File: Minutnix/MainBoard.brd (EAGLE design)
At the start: 108.8 x 69.7 mm, 32 parts, among them IC1 MEGA8-AI, Q1 32.768kHz

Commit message: Archivisation and actualisation
Archivisation of 1 version of boards
New version of boards
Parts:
- removed DRIVER1, DRIVER2: 74LS47N, 74xx-eu:DIL16
- added C5, C6, C7, C8: 0.1uF, rcl:140CLH-1010
- added IC2, IC3, IC4, IC5: TPIC6C596PW, tpic:SO16
- added LSDIGIT1, MSDIGIT1: LED-7-SEGM-56MM, BigLED7Segm:MYTHT
- added Q2: (no value), semicon-smd-ipc:SOT23
- added R16, R17, R18, R19, R20, R21, R22, R23, R24, R25, R26, R27, R28: 50, rcl:R01005
- added R29: 10k, rcl:R01005
- added R30: 4.7k, rcl:R01005
- added SG1: F/CM12P, buzzer:F/CM12P
- moved R15 121.8 mm to (100.0, -92.8), turned to 0 degrees
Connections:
- removed net N$33: IC1.9, R15.2
- removed net N$36: J_REG_9V_1.VOUT, LSDIGIT.COM1, LSDIGIT.COM8, MSDIGIT.COM1, MSDIGIT.COM8
- new net N$43: IC2.14, R8.2
- new net N$51: MSDIGIT1.A, R22.1
- new net N$52: MSDIGIT1.B, R23.1
- new net N$53: MSDIGIT1.C, R24.1
- new net N$54: MSDIGIT1.D, R25.1
- new net N$55: MSDIGIT1.E, R26.1
- new net N$56: MSDIGIT1.F, R27.1
- new net N$57: MSDIGIT1.G, R28.1
- new net N$58: IC3.3, R9.2
- new net N$59: IC3.4, R10.2
- new net N$60: IC3.5, R11.2
- new net N$61: IC3.6, R12.2
- new net N$62: IC3.11, R13.2
- new net N$63: IC3.12, R14.2
- new net N$64: IC3.13, R15.2
- new net N$65: IC3.14, R16.2
- new net N$66: IC4.3, R17.2
- new net N$67: IC4.4, R18.2
- new net N$68: IC4.5, R19.2
- new net N$69: IC4.6, R20.2
- new net N$70: IC4.11, R21.2
- new net N$71: IC4.12, R22.2
- new net N$72: IC4.13, R23.2
- new net N$73: IC4.14, R24.2
- new net N$74: IC5.3, R25.2
- new net N$75: IC5.4, R26.2
- new net N$76: IC5.5, R27.2
- new net N$77: IC5.6, R28.2
- new net N$78: IC3.9, IC4.2
- new net N$79: IC4.9, IC5.2
- new net N$80: IC2.9, IC3.2
- net GND: now also C5.-, C6.-, C7.-, C8.-, IC2.16, IC3.16, IC4.16, IC5.16, Q2.2; no longer DRIVER1.8, DRIVER2.8
- net N$10: now also IC2.12; no longer DRIVER1.15
- net N$11: now also IC2.13; no longer DRIVER1.14
- net N$21: now also Q2.1, R30.1; no longer DRIVER2.6, IC1.17, USBASP.3
- net N$23: now also IC2.2; no longer DRIVER2.1, USBASP.4
- net N$24: now also IC2.7, IC3.7, IC4.7, IC5.7, R29.1; no longer DRIVER2.2, IC1.16, USBASP.1
- net N$26: now also IC1.17, IC2.15, IC3.15, IC4.15, IC5.15, USBASP.3; no longer DRIVER1.7, IC1.23
- net N$27: now also IC1.16, IC2.10, IC3.10, IC4.10, IC5.10, USBASP.1; no longer DRIVER1.1, IC1.24
- net N$28: now also J_REG_9V_1.VOUT, LSDIGIT.COM1, LSDIGIT.COM8, LSDIGIT1.COM1, LSDIGIT1.COM8, MSDIGIT.COM1, MSDIGIT.COM8, MSDIGIT1.COM1, MSDIGIT1.COM8; no longer DRIVER1.2, IC1.25
- net N$29: now also Q2.3, SG1.-; no longer DRIVER1.6, IC1.26
- net N$3: now also IC1.13, R30.2; no longer DRIVER2.7, IC1.12
- net N$32: no longer R15.1
- net N$4: now also IC1.14, IC2.8, IC3.8, IC4.8, IC5.8; no longer DRIVER1.4, DRIVER2.4, IC1.13
- net N$44: now also LSDIGIT1.A, R15.1; no longer DRIVER2.14, R14.2
- net N$45: now also LSDIGIT1.B, R16.1; no longer DRIVER2.15, R13.2
- net N$46: now also LSDIGIT1.C, R17.1; no longer DRIVER2.9, R12.2
- net N$47: now also LSDIGIT1.D, R18.1; no longer DRIVER2.10, R11.2
- net N$48: now also LSDIGIT1.E, R19.1; no longer DRIVER2.11, R10.2
- net N$49: now also LSDIGIT1.F, R20.1; no longer DRIVER2.12, R9.2
- net N$5: now also IC2.3; no longer DRIVER1.13
- net N$50: now also LSDIGIT1.G, R21.1; no longer DRIVER2.13, R8.2
- net N$6: now also IC2.4; no longer DRIVER1.12
- net N$7: now also IC2.5; no longer DRIVER1.11
- net N$8: now also IC2.6; no longer DRIVER1.10
- net N$9: now also IC2.11; no longer DRIVER1.9
- net VCC: now also C5.+, C6.+, C7.+, C8.+, IC2.1, IC3.1, IC4.1, IC5.1, R29.2, SG1.+; no longer DRIVER1.16, DRIVER2.16
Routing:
- net N$36: track 205.8 -> 0.00 mm
- net N$28: track 0.00 -> 198.0 mm
- net N$45: track 49.2 -> 0.00 mm
- net N$44: track 43.9 -> 0.00 mm
- net N$50: track 43.6 -> 0.00 mm
- net N$46: track 41.9 -> 0.00 mm
- net N$49: track 41.8 -> 0.00 mm
- net N$3: track 37.9 -> 0.00 mm
- net N$47: track 27.8 -> 0.00 mm
- net N$4: track 26.8 -> 0.00 mm
- net N$48: track 23.4 -> 0.00 mm
- net VCC: track 151.9 -> 130.9 mm
- net N$21: track 13.4 -> 0.00 mm
- net N$26: track 0.00 -> 12.8 mm
- net N$24: track 9.69 -> 0.00 mm
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
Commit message: Minor board changes
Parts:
- removed EKSP: (no value), con-harting-ml:ML6
- added C10: 0.1uF, rcl:140CLH-1010
- added C9: (no value), rcl:140CLH-1010
- added GND, PAD1, PAD10, PAD11, PAD12, PAD13, PAD14, PAD2, PAD3, PAD4, PAD5, PAD6, PAD7, PAD8, PAD9, VCC: WIREPADSMD5-2,5, wirepad:5-2,5
- added LED1, LED2: (no value), led:LED5MM
- added PHOTORES: A1050_09, photo-elements:T0-46-A10XX
- added R31: 47k, rcl:R1206
- added R32: 7.05k, rcl:R1206
- added R33: 4.7k, rcl:R1206
- added R34, R35: 50, rcl:R1206
- added U$1: PCF8574AT, i2c:SO16
- R0, R1, R10, R11, R12, R13, R14, R15, R16, R17, R18, R19, R2, R20, R21, R22, R23, R24, R25, R26, R27, R28, R29, R3, R30, R4, R5, R6, R7, R8, R9: device rcl:R01005 -> rcl:R1206
- moved Q2 427.4 mm to (-21.6, 180.3)
- moved C7 390.5 mm to (-139.7, 146.1)
- moved R29 380.7 mm to (13.9, 170.0)
- moved SG1 376.6 mm to (-20.3, 148.6)
- moved C6 374.4 mm to (-125.7, 146.1)
- moved C8 373.5 mm to (-20.3, 163.8)
- moved C5 358.5 mm to (-111.8, 146.1)
- moved R30 327.9 mm to (53.6, 93.3)
- moved R23 241.7 mm to (134.8, 64.6), turned to 270 degrees
- moved Q1 240.9 mm to (-81.3, 172.7), flipped to the top, turned to 0 degrees
- moved C4 235.9 mm to (-97.8, 146.1), flipped to the top
- moved R27 234.2 mm to (126.9, 64.6), turned to 270 degrees
- moved R28 232.6 mm to (124.2, 64.6), turned to 270 degrees
- moved U$3 214.3 mm to (-58.9, 1.83), flipped to the top
- moved C3 213.0 mm to (-83.8, 146.1), flipped to the top, turned to 0 degrees
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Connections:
- new net N$33: IC1.27, U$1.15
- new net N$36: IC1.32, U$1.13
- new net N$81: IC1.28, U$1.14
- new net N$82: IC1.26, PAD11.1
- new net N$83: IC1.12, PAD9.1
- new net N$84: IC1.9, PAD10.1
- new net N$85: PAD1.1, U$1.4
- new net N$86: PAD2.1, U$1.5
- new net N$87: PAD3.1, U$1.6
- new net N$88: PAD4.1, U$1.7
- new net N$89: PAD5.1, U$1.9
- new net N$90: PAD6.1, U$1.10
- new net N$91: PAD7.1, U$1.11
- new net N$92: PAD8.1, U$1.12
- new net N$93: IC1.19, PHOTORES.2, R31.1
- new net N$94: LED1.K, R34.1
- new net N$95: LED2.K, R35.1
- new net N$96: IC3.13, R34.2
- new net N$97: IC3.14, R35.2
- net GND: now also C10.-, C9.-, GND.1, PHOTORES.1, R32.2, U$1.1, U$1.2, U$1.3, U$1.8; no longer EKSP.6
- net N$12: now also IC1.23, PAD14.1; no longer EKSP.1, IC1.27
- net N$14: now also IC1.24, PAD13.1; no longer EKSP.5, IC1.32
- net N$20: now also IC1.25, PAD12.1; no longer EKSP.3, IC1.28
- net N$28: now also R31.2
- net N$32: now also C10.+, IC1.20, R32.1, R33.2; no longer LSDIGIT.DP
- net N$64: now also IC4.3; no longer IC3.13
- net N$65: now also IC4.4; no longer IC3.14
- net N$66: now also IC4.5; no longer IC4.3
- net N$67: now also IC4.6; no longer IC4.4
- net N$68: now also IC4.11; no longer IC4.5
- net N$69: now also IC4.12; no longer IC4.6
- net N$70: now also IC4.13; no longer IC4.11
- net N$71: now also IC4.14; no longer IC4.12
- net N$72: now also IC5.3; no longer IC4.13
- net N$73: now also IC5.4; no longer IC4.14
- net N$74: now also IC5.5; no longer IC5.3
- net N$75: now also IC5.6; no longer IC5.4
- net N$76: now also IC5.11; no longer IC5.5
- net N$77: now also IC5.12; no longer IC5.6
- net VCC: now also C9.+, LED1.A, LED2.A, R33.1, U$1.16, VCC.1; no longer EKSP.2
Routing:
- net N$28: track 198.0 -> 0.00 mm
- net VCC: track 130.9 -> 0.00 mm, vias 2 -> 0
- net GND: track 75.4 -> 0.00 mm
- net N$35: track 31.2 -> 0.00 mm
- net N$26: track 12.8 -> 0.00 mm
- net N$1: track 7.71 -> 0.00 mm
- net N$2: track 7.37 -> 0.00 mm
- net N$23: track 3.88 -> 0.00 mm
- net N$41: track 1.86 -> 0.00 mm
- net N$42: track 1.84 -> 0.00 mm
- net N$18: track 1.72 -> 0.00 mm
- net N$17: track 1.68 -> 0.00 mm
- net N$16: track 1.65 -> 0.00 mm
- net N$13: track 1.45 -> 0.00 mm
- net N$15: track 1.43 -> 0.00 mm
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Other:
- board size 108.8 x 69.7 mm -> 206.2 x 74.7 mm

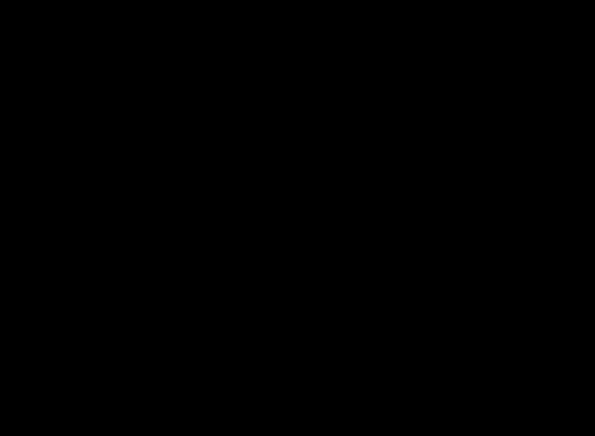
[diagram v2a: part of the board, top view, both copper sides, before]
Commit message: Pullup for displays
+removed trash
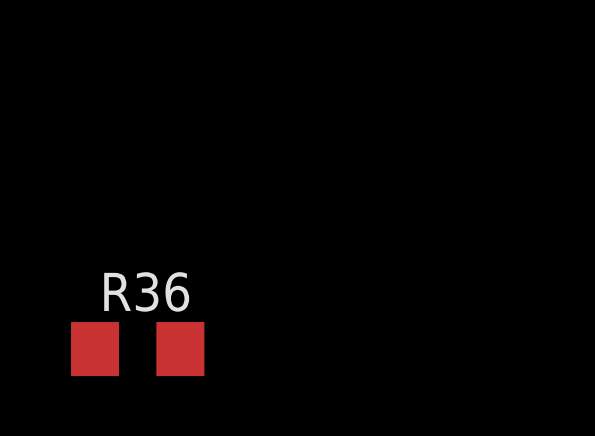
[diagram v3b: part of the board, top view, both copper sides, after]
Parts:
- added R36: 5k, rcl:R1206
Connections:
- net N$4: now also R36.1
- net VCC: now also R36.2
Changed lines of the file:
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@@
 <attribute name="VALUE" x="108.53" y="40.46" size="1.27" layer="27"/>
+</element>
+<element name="R36" library="rcl" library_urn="urn:adsk.eagle:library:334" package="R1206" value="5k" x="-144.6" y="-20.7" smashed="yes">
+<attribute name="NAME" x="-145.87" y="-19.43" size="1.27" layer="25"/>
+<attribute name="SPICEPREFIX" value="R" x="-144.6" y="-20.7" size="1.778" layer="27" display="off"/>
+<attribute name="VALUE" x="-145.87" y="-23.24" size="1.27" layer="27"/>
 </element>
 </elements>
@@
 <contactref element="LED1" pad="A"/>
 <contactref element="LED2" pad="A"/>
+<contactref element="R36" pad="2"/>
 <wire x1="134.345" y1="43.1666" x2="183.345" y2="42.5066" width="0" layer="19" extent="16-16"/>
 <wire x1="101.93" y1="43.1" x2="134.345" y2="43.1666" width="0" layer="19" extent="16-16"/>
@@
 <wire x1="-135.195" y1="165.7334" x2="-135.55" y2="146.05" width="0" layer="19" extent="1-1"/>
 <wire x1="-48.12753125" y1="8.811065625" x2="34.465" y2="42.1766" width="0" layer="19" extent="16-16"/>
+<wire x1="-143.178" y1="-20.7" x2="-48.12753125" y2="8.811065625" width="0" layer="19" extent="1-1"/>
 </signal>
 <signal name="N$22">
@@
 <contactref element="IC2" pad="8"/>
 <contactref element="IC1" pad="14"/>
+<contactref element="R36" pad="1"/>
 <wire x1="125.455" y1="43.1666" x2="174.455" y2="42.5066" width="0" layer="19" extent="16-16"/>
 <wire x1="71.715" y1="43.1666" x2="125.455" y2="43.1666" width="0" layer="19" extent="16-16"/>
 <wire x1="25.575" y1="42.1766" x2="71.715" y2="43.1666" width="0" layer="19" extent="16-16"/>
 <wire x1="-58.49" y1="141.7574" x2="25.575" y2="42.1766" width="0" layer="19" extent="1-16"/>
+<wire x1="-146.022" y1="-20.7" x2="25.575" y2="42.1766" width="0" layer="19" extent="1-16"/>
 </signal>
 <signal name="N$24">
 <contactref element="IC3" pad="7"/>
 <contactref element="IC2" pad="7"/>
-<contactref element="IC4" pad="7"/>
 <contactref element="R29" pad="1"/>
 <contactref element="IC5" pad="7"/>
+<contactref element="IC4" pad="7"/>
 <wire x1="126.725" y1="43.1666" x2="175.725" y2="42.5066" width="0" layer="19" extent="16-16"/>
 <wire x1="72.985" y1="43.1666" x2="126.725" y2="43.1666" width="0" layer="19" extent="16-16"/>

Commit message: new lib + board progress
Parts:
- removed C5, C6, C7, C8: 0.1uF, rcl:140CLH-1010
- removed C9: (no value), rcl:140CLH-1010
- removed GND, PAD1, PAD10, PAD11, PAD12, PAD13, PAD14, PAD2, PAD3, PAD4, PAD5, PAD6, PAD7, PAD8, PAD9, VCC: WIREPADSMD5-2,5, wirepad:5-2,5
- removed IC2, IC3, IC4, IC5: TPIC6C596PW, tpic:SO16
- removed J_REG_9V_1: 9V_VOLTAGE_REGULATOR, PololuVreg:9V_VOLTAGE_REGULATOR
- removed LED1, LED2: (no value), led:LED5MM
- removed LSDIGIT, LSDIGIT1, MSDIGIT, MSDIGIT1: LED-7-SEGM-56MM, BigLED7Segm:MYTHT
- removed Q1: 32.768kHz, crystal:TC26V
- removed R0: 4.7k, rcl:R1206
- removed R32: 7.05k, rcl:R1206
- removed R35: 50, rcl:R1206
- removed SHOTTKYDIODE: S2A, s2x_10:DO214AA
- removed U$1: PCF8574AT, i2c:SO16
- removed U$3: BATTERY-CHARGER-LI-PROT, diy-modules:BATTERY-CHARGER-LI-PROT
- removed UART: (no value), pinhead:1X04
- removed USBASP: (no value), con-harting-ml:ML6
- added ATMEGA328P: ATMEGA328P-AU, atmega328:QFP80P900X900X120-32N
- added C11: 10u, capacitor-wima:C2.5-2
- added C12, C13: 0.1u, capacitor-wima:C2.5-2
- added C14, C15, C16, C17, C18: 100n, rcl:C0603
- added C24: 10pF, capacitor-wima:C2.5-2
- added C25: 10 - 22uF, capacitor-wima:C2.5-2
- added C26: 56nF, capacitor-wima:C2.5-2
- added C27: 4.7u, capacitor-wima:C2.5-2
- added C29, C30: 22pF, rcl:C0603
- added C31: 470uF, rcl:153CLV-0810
- added C32: 100uF, rcl:140CLH-1010
- added COLON1, COLON2: (no value), led:LED5MM
- added EXPANDER: PCF8574AT, i2c:SO16
- added IC6: TP4056, TP4056:SOP-8
- added IC7: FT232RL, ftdi:SSOP28
- added IC9: SC4503, v-reg-3:SOT23-5
- added JP1, JP10, JP12, JP13, JP14, JP15, JP16, JP17, JP18, JP19, JP2, JP20, JP3, JP4, JP5, JP6, JP7, JP8, JP9: (no value), pinhead:1X01
- added L1: 10uH, inductors:DR73
- added L3: 4.237H, inductor-neosid:MS42
- added LED3, LED4, RXLED, TXLED: (no value), led:CHIPLED_0603
- added LSDIGIT_MINUTES, LSDIGIT_SECONDS, MSDIGIT_MINUTES, MSDIGIT_SECONDS: LED-7-SEGM-56MM, BigLED7Segm:MYTHT
- added LS_MIN_REG, LS_SEC_REG, MS_MIN_REG, MS_SEC_REG: TPIC6C596PW, tpic:SO16
- added Q4: 32.768kHz, crystal_clock:CRYSTAL-SMD-2X6-CYL
- added R37, R38, R39: 1k, rcl:R1206
- added R40: 100, rcl:R1206
- added R41: 1.2k, rcl:R1206
- added R42, R43, R44, R45, R46, R56, R61: 4.7k, rcl:R0603
- added R47, R52, R64, R65, R66: 2k2, rcl:R0603
- added R50: 400R, rcl:R0603
- added R53: 15k, rcl:R1206
- added R54: 620k, rcl:R1206
- added R55: 100k, rcl:R1206
- added R57: (no value), rcl:RTRIM3296Y
- added S1: (no value), switch:MS243
- added SHOTTKYDIODE2, SHOTTKYDIODE3: S2A, s2x_10:DO214AA
- added SJ1: (no value), jumper:SJ
- added SPI_JUMPERS: (no value), con-lstb:MA03-2
- added T1: DMN3024LSD, FS8205A:TSSOP-8
- added U$2: DW01A, DW01A:SOT23-6
- added X1: FH12-12S-0.5SH, con-hirose:FH12-12S-0.5SH
- added X2, X3: 87438-03, con-molex:87438-03
- C1, C2: value 22pF -> 100n; device capacitor-wima:C2.5-2 -> rcl:C0603
- C10: value 0.1uF -> 100n; device rcl:140CLH-1010 -> rcl:C0603
- C3: value 470uF -> 4.7u; device rcl:140CLH-1010 -> rcl:C3216
- C4: value 100uF -> 100n; device rcl:140CLH-1010 -> rcl:C0603
- PHOTORES: value A1050_09 -> VT90N1; device photo-elements:T0-46-A10XX -> photo-elements:VT900
- R1, R10, R11, R12, R13, R14, R15, R16, R17, R18, R19, R2, R20, R21, R22, R23, R24, R25, R26, R27, R28, R29, R3, R30, R33, R4, R5, R6, R7, R8, R9: device rcl:R1206 -> rcl:R0603
- R31: value 47k -> 4.7k; device rcl:R1206 -> rcl:R0603
- R34: value 50 -> 400R; device rcl:R1206 -> rcl:R0603
- R36: value 5k -> 4.7k; device rcl:R1206 -> rcl:R0603
- SG1: value F/CM12P -> F/HGP; device buzzer:F/CM12P -> buzzer:F/HGP
- moved R19 320.5 mm to (-97.8, 184.2), turned to 0 degrees
- moved R18 318.5 mm to (-92.7, 184.2), turned to 0 degrees
- moved R17 316.4 mm to (-87.6, 184.2), turned to 0 degrees
- moved R26 311.0 mm to (-133.3, 184.2), turned to 0 degrees
- moved R25 309.0 mm to (-128.3, 184.2), turned to 0 degrees
- moved R24 306.9 mm to (-123.2, 184.2), turned to 0 degrees
- moved R21 304.4 mm to (-108.0, 184.2), turned to 0 degrees
- moved R20 302.2 mm to (-102.9, 184.2), turned to 0 degrees
- moved R28 293.1 mm to (-143.5, 184.2), turned to 0 degrees
- moved R27 291.0 mm to (-138.4, 184.2), turned to 0 degrees
- moved R16 291.0 mm to (-82.5, 184.2), turned to 0 degrees
- moved R15 283.9 mm to (-77.5, 184.2), turned to 0 degrees
- moved R23 279.8 mm to (-118.1, 184.2), turned to 0 degrees
- moved R22 272.7 mm to (-113.0, 184.2), turned to 0 degrees
- moved R36 241.6 mm to (-16.5, 184.2)
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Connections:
- removed net N$1: C1.2, IC1.7, Q1.2
- removed net N$27: IC1.16, IC2.10, IC3.10, IC4.10, IC5.10, USBASP.1
- removed net N$29: Q2.3, SG1.-
- removed net N$49: LSDIGIT1.F, R20.1
- removed net N$52: MSDIGIT1.B, R23.1
- removed net N$53: MSDIGIT1.C, R24.1
- removed net N$54: MSDIGIT1.D, R25.1
- removed net N$55: MSDIGIT1.E, R26.1
- removed net N$56: MSDIGIT1.F, R27.1
- removed net N$65 (its old number): IC4.4, R16.2
- removed net N$81: IC1.28, U$1.14
- removed net N$82: IC1.26, PAD11.1
- removed net N$83: IC1.12, PAD9.1
- removed net N$84: IC1.9, PAD10.1
- removed net N$85: PAD1.1, U$1.4
- removed net N$86: PAD2.1, U$1.5
- removed net N$87: PAD3.1, U$1.6
- removed net N$88: PAD4.1, U$1.7
- removed net N$89: PAD5.1, U$1.9
- removed net N$90: PAD6.1, U$1.10
- removed net N$91: PAD7.1, U$1.11
- removed net N$92: PAD8.1, U$1.12
- removed net N$93: IC1.19, PHOTORES.2, R31.1
- removed net N$97: IC3.14, R35.2
- new net +3V3: C1.2, IC7.17, RXLED.A, TXLED.A
- new net +5V: C12.2, C2.2, C3.1, IC6.4, IC6.8, IC7.20, IC7.4, LED3.A, LED4.A, X2.1
- new net AREF: ATMEGA328P.20, C4.1, IC1.20
- new net AVCC: ATMEGA328P.18, C32.+, IC1.18, L1.1
- new net BATTERY+: C11.2, IC6.5, R40.1, S1.1, X3.1
- new net BATTERY-: C13.1, T1.6, T1.7, U$2.6, X3.3
- new net BATTERY_S: JP20.1, X3.2
- new net BUZZ: ATMEGA328P.13, IC1.13, R30.2
- new net CBUS2: IC7.13, JP17.1
- new net CBUS3: IC7.14, JP18.1
- new net CBUS4: IC7.12, JP19.1
- new net COUNTER: EXPANDER.6, R44.2, X1.3
- new net CTS: IC7.11, JP10.1
- new net DCD: IC7.10, JP15.1
- new net DI: JP16.1
- new net DSR: IC7.9, JP12.1
- new net DTR: C10.2, IC7.2
- new net D_BLOCK: ATMEGA328P.14, IC1.14, LS_MIN_REG.8, LS_SEC_REG.8, MS_MIN_REG.8, MS_SEC_REG.8, R36.1
- new net D_RCK: ATMEGA328P.12, IC1.12, LS_MIN_REG.10, LS_SEC_REG.10, MS_MIN_REG.10, MS_SEC_REG.10
- new net D_SCK: ATMEGA328P.17, IC1.17, LS_MIN_REG.15, LS_SEC_REG.15, MS_MIN_REG.15, MS_SEC_REG.15, SPI_JUMPERS.4
- new net D_SI: ATMEGA328P.15, IC1.15, LS_SEC_REG.2, SPI_JUMPERS.3
- new net ENC_A: EXPANDER.10, R33.2, X1.6
- new net ENC_B: EXPANDER.11, R31.2, X1.7
- new net EXP_INT: ATMEGA328P.32, EXPANDER.13, IC1.32
- new net EXP_SCL: ATMEGA328P.28, EXPANDER.14, IC1.28
- new net EXP_SDA: ATMEGA328P.27, EXPANDER.15, IC1.27
- new net FTRESET: IC7.19, JP7.1
- new net GNDA: ATMEGA328P.21, IC1.21
- new net LIGHT_SENS: ATMEGA328P.23, IC1.23, PHOTORES.2, R57.2
- new net L_COUNTER: ATMEGA328P.24, IC1.24, R52.2
- new net L_VOLUME: ATMEGA328P.26, IC1.26, R64.2
- new net L_WARNING: ATMEGA328P.25, IC1.25, R47.2
- new net MISO: ATMEGA328P.16, IC1.16, SPI_JUMPERS.6
- new net N$100: LED3.C, R37.2
- new net N$101: LED4.C, R38.2
- new net N$102: T1.4, U$2.3
- new net N$104: T1.1, T1.8
- new net N$105: T1.5, U$2.1
- new net N$106: R39.2, U$2.2
- new net N$109: C13.2, R40.2, U$2.5
- new net N$111: IC6.2, R41.2
- new net N$113: IC9.1, L3.1, SHOTTKYDIODE2.A
- new net N$118: C26.2, IC9.4, R53.2
- new net N$119: C24.1, IC9.3, R54.2, R55.1
- new net N$21: MSDIGIT_MINUTES.D, R24.1
- new net N$98: IC6.7, R37.1
- new net N$99: IC6.6, R38.1
- new net OSCO: IC7.28, JP8.1
- new net PLAY/PAUSE: EXPANDER.5, R45.2, X1.2
- new net RESET: ATMEGA328P.29, C10.1, IC1.29, R56.1, SPI_JUMPERS.2
- new net RI: IC7.6
- new net RTS: IC7.3, JP9.1
- new net RXD: ATMEGA328P.30, IC1.30, IC7.1
- new net STOP/RESET: EXPANDER.4, R46.2, X1.1
- new net S_VCC: ATMEGA328P.11, ATMEGA328P.4, ATMEGA328P.6, C31.+, IC1.11, IC1.4, IC1.6, L1.2, SHOTTKYDIODE3.C, SPI_JUMPERS.5
- new net TXD: ATMEGA328P.31, IC1.31, IC7.5
- new net UA1: ATMEGA328P.1, IC1.1, JP1.1
- new net UA2: ATMEGA328P.2, IC1.2, JP2.1
- new net UA3: ATMEGA328P.9, IC1.9, JP3.1
- new net UA4: ATMEGA328P.19, IC1.19, JP4.1
- new net UA5: ATMEGA328P.22, IC1.22, JP5.1
- new net UD1: JP13.1, LS_SEC_REG.14
- new net UD2: JP14.1, MS_MIN_REG.14
- new net UP1: EXPANDER.12, JP6.1, SJ1.1
- new net USBDM: IC7.16, X1.11
- new net USBDP: IC7.15, X1.12
- new net VDD: C24.2, C25.2, R54.1, R57.1, SHOTTKYDIODE2.C
- new net VDD1: LSDIGIT_MINUTES.COM1, LSDIGIT_MINUTES.COM8, LSDIGIT_SECONDS.COM1, LSDIGIT_SECONDS.COM8, MSDIGIT_MINUTES.COM1, MSDIGIT_MINUTES.COM8, MSDIGIT_SECONDS.COM1, MSDIGIT_SECONDS.COM8
- new net VOLUME: EXPANDER.9, R42.2, X1.5
- new net WARNING: EXPANDER.7, R43.2, X1.4
- new net XTAL1: ATMEGA328P.7, C29.2, IC1.7, Q4.X2
- new net XTAL2: ATMEGA328P.8, C30.2, IC1.8, Q4.X1
- net GND: now also ATMEGA328P.3, ATMEGA328P.5, C11.1, C12.1, C14.1, C15.1, C16.1, C17.1, C18.1, C25.1, C26.1, C27.1, C29.1, C3.2, C30.1, C31.-, C32.-, C4.2, EXPANDER.1, EXPANDER.2, EXPANDER.3, EXPANDER.8, IC6.1, IC6.3, IC7.18, IC7.21, IC7.25, IC7.26, IC7.7, IC9.2, LS_MIN_REG.16, LS_SEC_REG.16, MS_MIN_REG.16, MS_SEC_REG.16, R39.1, R41.1, R55.2, SPI_JUMPERS.1, T1.2, T1.3, X2.2; no longer C10.-, C3.-, C4.-, C5.-, C6.-, C7.-, C8.-, C9.-, GND.1, IC1.21, IC2.16, IC3.16, IC4.16, IC5.16, J_REG_9V_1.GND, R32.2, U$1.1, U$1.2, U$1.3, U$1.8, U$3.OUT-, UART.2, USBASP.6
- net N$10: now also LS_SEC_REG.12, R16.2; no longer IC2.12, R6.2
- net N$11: now also LS_SEC_REG.13, R15.2; no longer IC2.13, R7.2
- net N$12: now also R64.1, X1.10; no longer IC1.23, PAD14.1
- net N$13: now also LSDIGIT_MINUTES.G; no longer LSDIGIT.A
- net N$14: now also MSDIGIT_MINUTES.E, R23.1; no longer IC1.24, PAD13.1
- net N$15: now also LSDIGIT_MINUTES.F; no longer LSDIGIT.B
- net N$16: now also LSDIGIT_MINUTES.E; no longer LSDIGIT.C
- net N$17: now also LSDIGIT_MINUTES.D; no longer LSDIGIT.D
- net N$18: now also LSDIGIT_MINUTES.C; no longer LSDIGIT.E
- net N$19: now also LSDIGIT_MINUTES.B; no longer LSDIGIT.F
- net N$2: now also MS_SEC_REG.14, R50.2; no longer C2.2, IC1.8, Q1.1
- net N$20: now also LS_MIN_REG.14, R34.2; no longer IC1.25, PAD12.1
- net N$22: now also MS_MIN_REG.3, R27.2; no longer IC1.29, R0.1, USBASP.5
- net N$23: now also MSDIGIT_MINUTES.C, R25.1; no longer IC1.15, IC2.2
- net N$24: now also LS_MIN_REG.7, LS_SEC_REG.7, MS_MIN_REG.7, MS_SEC_REG.7; no longer IC2.7, IC3.7, IC4.7, IC5.7
- net N$25: now also LSDIGIT_MINUTES.A; no longer LSDIGIT.G
- net N$26: now also R47.1, X1.9; no longer IC1.17, IC2.15, IC3.15, IC4.15, IC5.15, USBASP.3
- net N$28: now also R52.1, X1.8; no longer J_REG_9V_1.VOUT, LSDIGIT.COM1, LSDIGIT.COM8, LSDIGIT1.COM1, LSDIGIT1.COM8, MSDIGIT.COM1, MSDIGIT.COM8, MSDIGIT1.COM1, MSDIGIT1.COM8, R31.2
- net N$3: now also MSDIGIT_MINUTES.F, R22.1; no longer IC1.13, R30.2
- net N$30: now also R61.2, SJ1.2; no longer IC1.31, UART.4
- net N$31: now also MSDIGIT_MINUTES.B, R26.1; no longer IC1.30, UART.3
- net N$32: now also MSDIGIT_MINUTES.A, R27.1; no longer C10.+, IC1.20, R32.1, R33.2
- net N$33: now also MSDIGIT_SECONDS.G, R8.1; no longer IC1.27, U$1.15
- net N$34: now also MSDIGIT_SECONDS.F, R9.1; no longer MSDIGIT.A, R8.1
- net N$35: now also MSDIGIT_SECONDS.E, R10.1; no longer C3.+, IC1.11, IC1.4, IC1.6, SHOTTKYDIODE.C
- net N$36: now also IC7.23, R66.2; no longer IC1.32, U$1.13
- net N$37: now also MSDIGIT_SECONDS.D, R11.1; no longer MSDIGIT.B, R9.1
- net N$38: now also MSDIGIT_SECONDS.C, R12.1; no longer MSDIGIT.C, R10.1
- net N$39: now also MSDIGIT_SECONDS.B, R13.1; no longer MSDIGIT.D, R11.1
- net N$4: now also MS_SEC_REG.3, R14.2; no longer IC1.14, IC2.8, IC3.8, IC4.8, IC5.8, R36.1
- net N$40: now also MSDIGIT_SECONDS.A, R14.1; no longer MSDIGIT.E, R12.1
- net N$41: now also LSDIGIT_SECONDS.G, R15.1; no longer MSDIGIT.F, R13.1
- net N$42: now also LSDIGIT_SECONDS.F, R16.1; no longer MSDIGIT.G, R14.1
- net N$43: now also IC7.22, R65.2; no longer IC2.14, R8.2
- net N$44: now also LSDIGIT_SECONDS.E, R17.1; no longer LSDIGIT1.A, R15.1
- net N$45: now also LSDIGIT_SECONDS.D, R18.1; no longer LSDIGIT1.B, R16.1
- net N$46: now also LSDIGIT_SECONDS.C, R19.1; no longer LSDIGIT1.C, R17.1
- net N$47: now also LSDIGIT_SECONDS.B, R20.1; no longer LSDIGIT1.D, R18.1
- net N$48: now also LSDIGIT_SECONDS.A, R21.1; no longer LSDIGIT1.E, R19.1
- net N$5: now also LS_SEC_REG.3, R21.2; no longer IC2.3, R1.2
- net N$50: now also COLON1.K, R50.1; no longer LSDIGIT1.G, R21.1
- net N$51: now also COLON2.K, R34.1; no longer MSDIGIT1.A, R22.1
- net N$57: now also MSDIGIT_MINUTES.G; no longer MSDIGIT1.G
- net N$58: now also MS_SEC_REG.4, R13.2; no longer IC3.3, R9.2
- net N$59: now also MS_SEC_REG.5, R12.2; no longer IC3.4, R10.2
- net N$6: now also LS_SEC_REG.4, R20.2; no longer IC2.4, R2.2
- net N$60: now also MS_SEC_REG.6; no longer IC3.5
- net N$61: now also MS_SEC_REG.11, R10.2; no longer IC3.6, R12.2
- net N$62: now also MS_SEC_REG.12, R9.2; no longer IC3.11, R13.2
- net N$63: now also MS_SEC_REG.13, R8.2; no longer IC3.12, R14.2
- net N$64: now also R66.1, TXLED.C; no longer IC4.3, R15.2
- net N$66: now also Q2.3, SG1.2; no longer IC4.5, R17.2
- net N$67: now also LS_MIN_REG.3, R7.2; no longer IC4.6, R18.2
- net N$68: now also LS_MIN_REG.4, R6.2; no longer IC4.11, R19.2
- net N$69: now also LS_MIN_REG.5, R5.2; no longer IC4.12, R20.2
- net N$7: now also LS_SEC_REG.5, R19.2; no longer IC2.5, R3.2
- net N$70: now also LS_MIN_REG.6, R4.2; no longer IC4.13, R21.2
- net N$71: now also LS_MIN_REG.11, R3.2; no longer IC4.14, R22.2
- net N$72: now also LS_MIN_REG.12, R2.2; no longer IC5.3, R23.2
- net N$73: now also LS_MIN_REG.13, R1.2; no longer IC5.4, R24.2
- net N$74: now also R65.1, RXLED.C; no longer IC5.5, R25.2
- net N$75: now also MS_MIN_REG.4; no longer IC5.6
- net N$76: now also MS_MIN_REG.5, R25.2; no longer IC5.11, R27.2
- net N$77: now also MS_MIN_REG.6, R24.2; no longer IC5.12, R28.2
- net N$78: now also LS_MIN_REG.2, MS_SEC_REG.9; no longer IC3.9, IC4.2
- net N$79: now also LS_MIN_REG.9, MS_MIN_REG.2; no longer IC4.9, IC5.2
- net N$8: now also LS_SEC_REG.6, R18.2; no longer IC2.6, R4.2
- net N$80: now also LS_SEC_REG.9, MS_SEC_REG.2; no longer IC2.9, IC3.2
- net N$9: now also LS_SEC_REG.11, R17.2; no longer IC2.11, R5.2
- net N$94: now also MS_MIN_REG.11, R23.2; no longer LED1.K, R34.1
- net N$95: now also MS_MIN_REG.12, R22.2; no longer LED2.K, R35.1
- net N$96: now also MS_MIN_REG.13, R28.2; no longer IC3.13, R34.2
- net VCC: now also ATMEGA328P.10, C14.2, C15.2, C16.2, C17.2, C18.2, C27.2, COLON1.A, COLON2.A, EXPANDER.16, IC9.5, L3.2, LS_MIN_REG.1, LS_SEC_REG.1, MS_MIN_REG.1, MS_SEC_REG.1, R31.1, R42.1, R43.1, R44.1, R45.1, R46.1, R53.1, R56.2, R61.1, S1.2, SG1.1, SHOTTKYDIODE3.A, X2.3; no longer C4.+, C5.+, C6.+, C7.+, C8.+, C9.+, IC1.18, IC2.1, IC3.1, IC4.1, IC5.1, J_REG_9V_1.VIN, LED1.A, LED2.A, R0.2, SG1.+, SHOTTKYDIODE.A, U$1.16, U$3.OUT+, UART.1, USBASP.2, VCC.1
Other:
- board size 206.2 x 74.7 mm -> 235 x 80 mm
